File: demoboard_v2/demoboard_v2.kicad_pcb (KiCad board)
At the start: 2 copper layers, 95.9 x 90.2 mm, 44 parts, among them J1 PC104-8BIT, P1 3v3_IN_CONNECTOR, P2 CONN_01X03, P3 CONN_01X03, P4 CONN_01X02, P5 CONN_01X02, Q1 DMN2075U, U1 TMS570LS0714, U2 AP7331, U3 AP7361_3.3v, U4 INA301

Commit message: Beginning board layout.
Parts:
- added C24: 0.1µF, SFUSat:C_0402, F.Cu at (126.8, 28.0)
- added C25: 0.1µF, SFUSat:C_0402, F.Cu at (139.0, 43.0)
- added C26: 0.1µF, SFUSat:C_0402, F.Cu at (160.0, 43.0)
- added C27: 33pF, SFUSat:C_0402, F.Cu at (135.0, 88.0)
- added C28: 33pF, SFUSat:C_0402, F.Cu at (139.0, 87.0)
- added C29: 10nF, SFUSat:C_0402, F.Cu at (149.4, 96.1)
- added C30: 470µF, SFUSat:Supercap_v2, F.Cu at (164.1, 90.9)
- added C31: 0.1µF, SFUSat:C_0402, F.Cu at (307.4, 93.8)
- added C32: 0.1µF, SFUSat:C_0402, F.Cu at (293.9, 105.9)
- added D1: LED, SFUSat:LED_0603, F.Cu at (265.5, 113.6)
- added D2: PESD5Zx, SFUSat:PESD57zx, F.Cu at (317.2, 104.8)
- added D3: LED, SFUSat:L_0402, F.Cu at (330.9, 90.3)
- added FLASH0_RESET: TEST_1P, SFUSat:Test_Point, F.Cu at (119.0, 24.0)
- added FLASH0_WP: TEST_1P, SFUSat:Test_Point, F.Cu at (114.0, 24.0)
- added FLASH_CS: FLASH_CS, SFUSat:3x_01In_Header_v2, F.Cu at (140.0, 24.0)
- added FLASH_SPI: FLASH_SPI, SFUSat:3x_01In_Header_v2, F.Cu at (128.0, 24.0)
- added P6: UART, SFUSat:2x01In_Header_v2, F.Cu at (325.3, 61.4)
- added P7: OSC_FUALT_INJECT, SFUSat:2x01In_Header_v2, F.Cu at (136.0, 96.0)
- added Q2: DMN2075U, SFUSat:SOT23_DMN2075U, F.Cu at (246.3, 94.7)
- added Q3: 1v2_GOOD, SFUSat:SOT23_DMN2075U, F.Cu at (244.4, 102.6)
- added Q4: DMN2075U, SFUSat:SOT23_DMN2075U, F.Cu at (327.2, 105.6)
- added Q5: DMN2075U, SFUSat:SOT23_DMN2075U, F.Cu at (318.3, 91.3)
- added R10: 10k, SFUSat:R_0402, F.Cu at (129.2, 43.5)
- added R11: 10k, SFUSat:R_0402, F.Cu at (122.0, 38.0)
- added R12: 0, SFUSat:R_0402, F.Cu at (122.0, 34.8)
- added R13: 10k, SFUSat:R_0402, F.Cu at (121.6, 31.6)
- added R14: 10k, SFUSat:R_0402, F.Cu at (264.9, 66.0)
- added R15: 10k, SFUSat:R_0402, F.Cu at (255.8, 78.4)
- added R16: 0, SFUSat:R_0402, F.Cu at (259.1, 76.9)
- added R17: 10k, SFUSat:R_0402, F.Cu at (259.1, 81.8)
- added R18: 10k, SFUSat:R_0402, F.Cu at (253.9, 83.3)
- added R19: 10k, SFUSat:R_0402, F.Cu at (250.6, 85.3)
- added R20: 0, SFUSat:R_0402, F.Cu at (264.9, 70.9)
- added R21: 10k, SFUSat:R_0402, F.Cu at (268.2, 66.0)
- added R22: 200k, SFUSat:R_0402, F.Cu at (297.6, 110.5)
- added R23: 187k, SFUSat:R_0402, F.Cu at (304.3, 104.1)
- added R24: 100k, SFUSat:R_0402, F.Cu at (293.6, 110.5)
- added R25: 10k, SFUSat:R_0402, F.Cu at (112.0, 83.0)
- added R26: 10k, SFUSat:R_0402, F.Cu at (324.3, 95.9)
- added R27: 100k, SFUSat:R_0402, F.Cu at (304.3, 99.3)
- added R28: 100k, SFUSat:R_0402, F.Cu at (301.7, 109.0)
- added R29: 100k, SFUSat:R_0402, F.Cu at (308.4, 103.3)
- added R30: 100k, SFUSat:R_0402, F.Cu at (308.4, 98.4)
- added R5: 10K, SFUSat:R_0402, F.Cu at (262.3, 108.9)
- added R6: 100, SFUSat:R_0402, F.Cu at (258.1, 114.1)
- added R7: 10k, SFUSat:R_0402, F.Cu at (327.3, 117.5)
- added R8: 10k, SFUSat:R_0402, F.Cu at (330.9, 95.5)
- added R9: 100, SFUSat:R_0402, F.Cu at (327.5, 95.9)
- added RTC_SPI: RTC_SPI, SFUSat:4x01In_Header_v2, F.Cu at (143.0, 105.0)
- added SW1: SPST, SFUSat:Tact_SW_SMD_v2, F.Cu at (275.4, 107.7)
- added SW2: SPST, SFUSat:Tact_SW_SMD_v2, F.Cu at (291.0, 95.6)
- added U5: FLASH_IS25LP016D, SFUSat:SOT-8_208mil_medium, F.Cu at (128.0, 35.0)
- added U6: FLASH_IS25LP016D, SFUSat:SOT-8_208mil_medium, F.Cu at (138.0, 35.0)
- added U7: FLASH_IS25LP016D, SFUSat:SOT-8_208mil_medium, F.Cu at (148.0, 35.0)
- added U8: AB-RTCMC-EOA9-S3, SFUSat:RTC_AB-RTCMC_EA09_S3, F.Cu at (144.2, 95.2)
- added U9: TPS3110, SFUSat:SOT_23_6, F.Cu at (288.2, 105.5)
- added W10: RTC_OE, SFUSat:Test_Point, F.Cu at (133.0, 105.0)
- added W11: RTC_INT, SFUSat:Test_Point, F.Cu at (128.0, 105.0)
- added W12: nERROR, SFUSat:Test_Point, F.Cu at (299.1, 99.9)
- added W13: WD_TEST, SFUSat:Test_Point, F.Cu at (326.0, 90.5)
- added W14: RESET_TEST, SFUSat:Test_Point, F.Cu at (300.5, 93.9)
- added W3: TEST_1P, SFUSat:Test_Point, F.Cu at (259.1, 61.5)
- added W4: TEST_1P, SFUSat:Test_Point, F.Cu at (250.6, 69.0)
- added W5: TEST_1P, SFUSat:Test_Point, F.Cu at (244.4, 75.1)
- added W6: TEST_1P, SFUSat:Test_Point, F.Cu at (235.9, 82.7)
- added W7: AD1EVT1, SFUSat:Test_Point, F.Cu at (317.5, 118.1)
- added W8: GIOB2, SFUSat:Test_Point, F.Cu at (323.3, 118.1)
- added W9: CLKOUT, SFUSat:Test_Point, F.Cu at (313.1, 70.6)
- added Y1: XTAL, SFUSat:SMD_XTAL, F.Cu at (137.0, 80.0)
- P2: value CONN_01X03 -> INA_INPUT
- P3: value CONN_01X03 -> INA_GND
- P4: value CONN_01X02 -> INA_EN
- P5: value CONN_01X02 -> INA_OUTPUT
- moved C1 200.8 mm to (263.4, 104.2)
- moved C2 199.4 mm to (254.9, 114.6)
- moved 1uF1 191.9 mm to (258.7, 109.4)
- moved C4 190.5 mm to (253.0, 99.0)
- moved C9 190.1 mm to (255.5, 104.2)
- moved C8 188.4 mm to (262.3, 99.0)
- moved C10 184.4 mm to (250.8, 104.2)
- moved C7 183.7 mm to (262.3, 93.8)
- moved C3 181.9 mm to (257.6, 93.8)
- moved C5 179.6 mm to (236.9, 113.1)
- moved C13 178.6 mm to (241.6, 109.7)
- moved C11 178.5 mm to (257.6, 99.0)
- moved C6 178.3 mm to (241.6, 114.9)
- moved C12 176.9 mm to (246.3, 109.7)
- moved C16 176.9 mm to (251.0, 109.4)
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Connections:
- J1 pad 10A: Net-(J1-Pad10A) -> RF_PWM1
- J1 pad 11A: Net-(J1-Pad11A) -> RF_PWM2
- J1 pad 17B: Net-(J1-Pad17B) -> I2C_SDA
- J1 pad 18B: Net-(J1-Pad18B) -> I2C_SCL
- J1 pad 1B: 104_GND -> 104_In_GND
- J1 pad 22A: (no net) -> Net-(J1-Pad22A)
- J1 pad 23A: (no net) -> Net-(J1-Pad23A)
- J1 pad 24A: (no net) -> Net-(J1-Pad24A)
- J1 pad 25A: (no net) -> Net-(J1-Pad25A)
- J1 pad 26A: (no net) -> Net-(J1-Pad26A)
- J1 pad 27A: (no net) -> Net-(J1-Pad27A)
- J1 pad 28A: (no net) -> Net-(J1-Pad28A)
- J1 pad 29A: (no net) -> Net-(J1-Pad29A)
- J1 pad 30A: (no net) -> Net-(J1-Pad30A)
- J1 pad 31A: (no net) -> Net-(J1-Pad31A)
- J1 pad 31B: 104_GND -> 104_In_GND
- J1 pad 32A: (no net) -> 104_In_GND
- J1 pad 32B: 104_GND -> 104_In_GND
- J1 pad 5B: Net-(J1-Pad5B) -> UART_RX
- J1 pad 6B: Net-(J1-Pad6B) -> UART_TX
- J1 pad 8A: Net-(J1-Pad8A) -> RF_ADC1
- J1 pad 9A: Net-(J1-Pad9A) -> RF_ADC2
- P1 pad 2: GND -> Net-(P1-Pad2)
- U1 pad 1: (no net) -> Net-(U1-Pad1)
- U1 pad 105: Net-(U1-Pad105) -> FLASH0_CS
- U1 pad 107: (no net) -> Net-(U1-Pad107)
- U1 pad 118: (no net) -> Net-(U1-Pad118)
- U1 pad 124: (no net) -> Net-(U1-Pad124)
- U1 pad 125: (no net) -> Net-(U1-Pad125)
- U1 pad 126: (no net) -> WATCHDOG
- U1 pad 127: (no net) -> Net-(U1-Pad127)
- U1 pad 130: Net-(U1-Pad130) -> FLASH1_CS
- U1 pad 133: (no net) -> Net-(U1-Pad133)
- U1 pad 139: (no net) -> Net-(U1-Pad139)
- U1 pad 140: (no net) -> RF_PWM1
- U1 pad 141: (no net) -> RF_PWM2
- U1 pad 142: (no net) -> Net-(U1-Pad142)
- U1 pad 15: (no net) -> Net-(U1-Pad15)
- U1 pad 16: (no net) -> GIOA6
- U1 pad 2: (no net) -> Net-(U1-Pad2)
- U1 pad 22: (no net) -> Net-(U1-Pad22)
- U1 pad 24: Net-(U1-Pad24) -> RTC_CS
- U1 pad 25: Net-(U1-Pad25) -> RTC_CLK
- U1 pad 3: (no net) -> I2C_SCL
- U1 pad 30: Net-(U1-Pad30) -> RTC_MOSI
- U1 pad 31: Net-(U1-Pad31) -> RTC_MISO
- U1 pad 33: (no net) -> Net-(U1-Pad33)
- U1 pad 35: (no net) -> Net-(U1-Pad35)
- U1 pad 36: (no net) -> Net-(U1-Pad36)
- U1 pad 38: (no net) -> UART_RX
- U1 pad 39: (no net) -> UART_TX
- U1 pad 4: (no net) -> I2C_SDA
- U1 pad 40: Net-(U1-Pad40) -> FLASH2_CS
- U1 pad 46: Net-(U1-Pad46) -> MASTER_RESET
- U1 pad 5: (no net) -> Net-(U1-Pad5)
- U1 pad 55: (no net) -> Net-(U1-Pad55)
- U1 pad 58: (no net) -> Net-(U1-Pad58)
- U1 pad 59: (no net) -> Net-(U1-Pad59)
- U1 pad 60: (no net) -> RF_ADC1
- U1 pad 61: (no net) -> Net-(U1-Pad61)
- U1 pad 62: (no net) -> Net-(U1-Pad62)
- U1 pad 63: (no net) -> Net-(U1-Pad63)
- U1 pad 64: (no net) -> Net-(U1-Pad64)
- U1 pad 65: (no net) -> Net-(U1-Pad65)
- U1 pad 66: (no net) -> 3v3
- U1 pad 67: (no net) -> GND
- U1 pad 68: (no net) -> GND
- U1 pad 69: (no net) -> 3v3
- U1 pad 70: (no net) -> Net-(U1-Pad70)
- U1 pad 71: (no net) -> RF_ADC2
- U1 pad 72: (no net) -> Net-(U1-Pad72)
- U1 pad 73: (no net) -> INA_OUT
- U1 pad 74: (no net) -> Net-(U1-Pad74)
- U1 pad 75: (no net) -> Net-(U1-Pad75)
- U1 pad 76: (no net) -> Net-(U1-Pad76)
- U1 pad 77: (no net) -> Net-(U1-Pad77)
- U1 pad 78: (no net) -> Net-(U1-Pad78)
- U1 pad 79: (no net) -> Net-(U1-Pad79)
- U1 pad 80: (no net) -> Net-(U1-Pad80)
- U1 pad 81: (no net) -> Net-(U1-Pad81)
- U1 pad 82: (no net) -> Net-(U1-Pad82)
- U1 pad 83: (no net) -> Net-(U1-Pad83)
- U1 pad 84: (no net) -> Net-(U1-Pad84)
- U1 pad 85: (no net) -> Net-(U1-Pad85)
- U1 pad 86: (no net) -> Net-(U1-Pad86)
- U1 pad 9: (no net) -> Net-(U1-Pad9)
- U1 pad 92: (no net) -> Net-(U1-Pad92)
- U1 pad 93: Net-(U1-Pad93) -> FLASH_MOSI
- U1 pad 94: Net-(U1-Pad94) -> FLASH_MISO
- U1 pad 95: Net-(U1-Pad95) -> FLASH_CLK
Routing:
- net FLASH0_CS: track 0.00 -> 40.2 mm, vias 0 -> 1
- net FLASH_MISO: track 0.00 -> 28.3 mm, vias 0 -> 1
- net Net-(R12-Pad2): track 0.00 -> 15.8 mm
- net 3v3: track 9.03 -> 23.5 mm
- net FLASH_CLK: track 0.00 -> 8.78 mm
- net FLASH_MOSI: track 0.00 -> 7.72 mm
- net Net-(R10-Pad1): track 0.00 -> 5.03 mm
- net GND: track 4.42 -> 8.48 mm, vias 3 -> 6

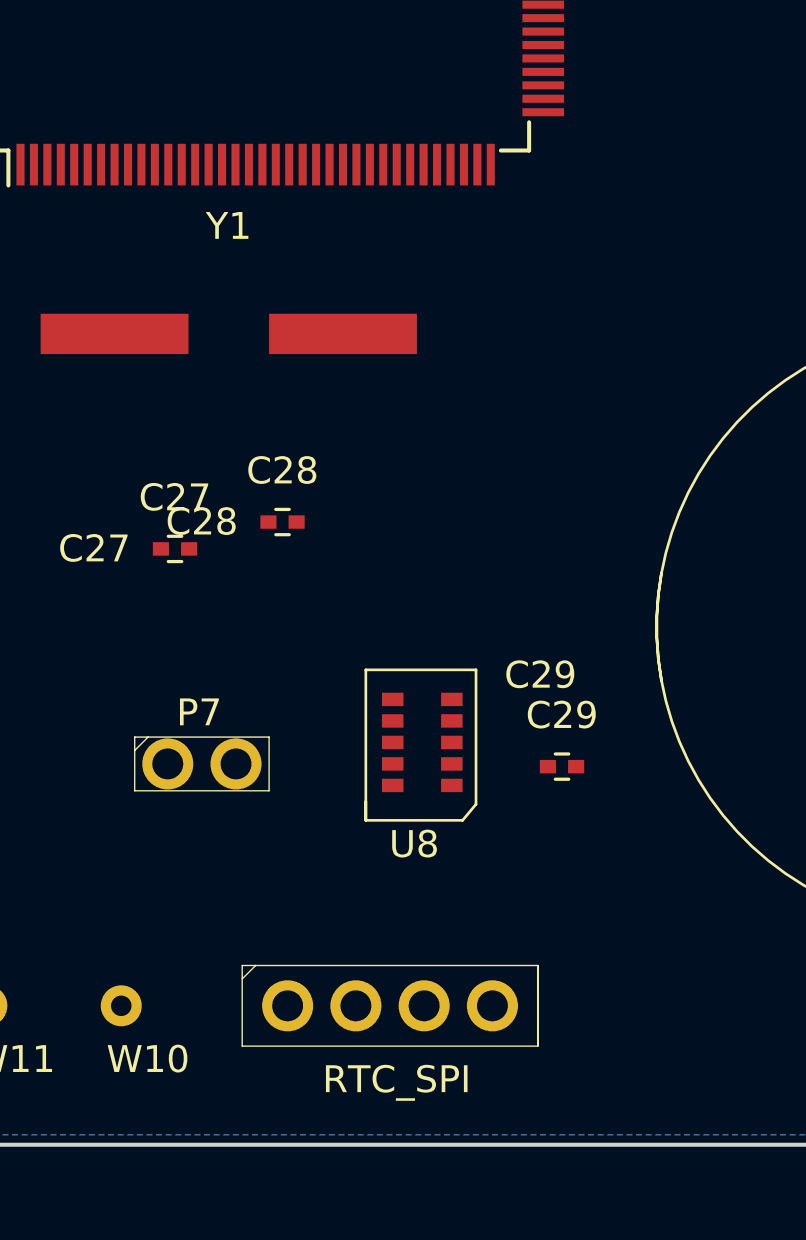
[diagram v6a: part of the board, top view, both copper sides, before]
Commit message: Connect RTC CS, CLK, MISO, MOSI
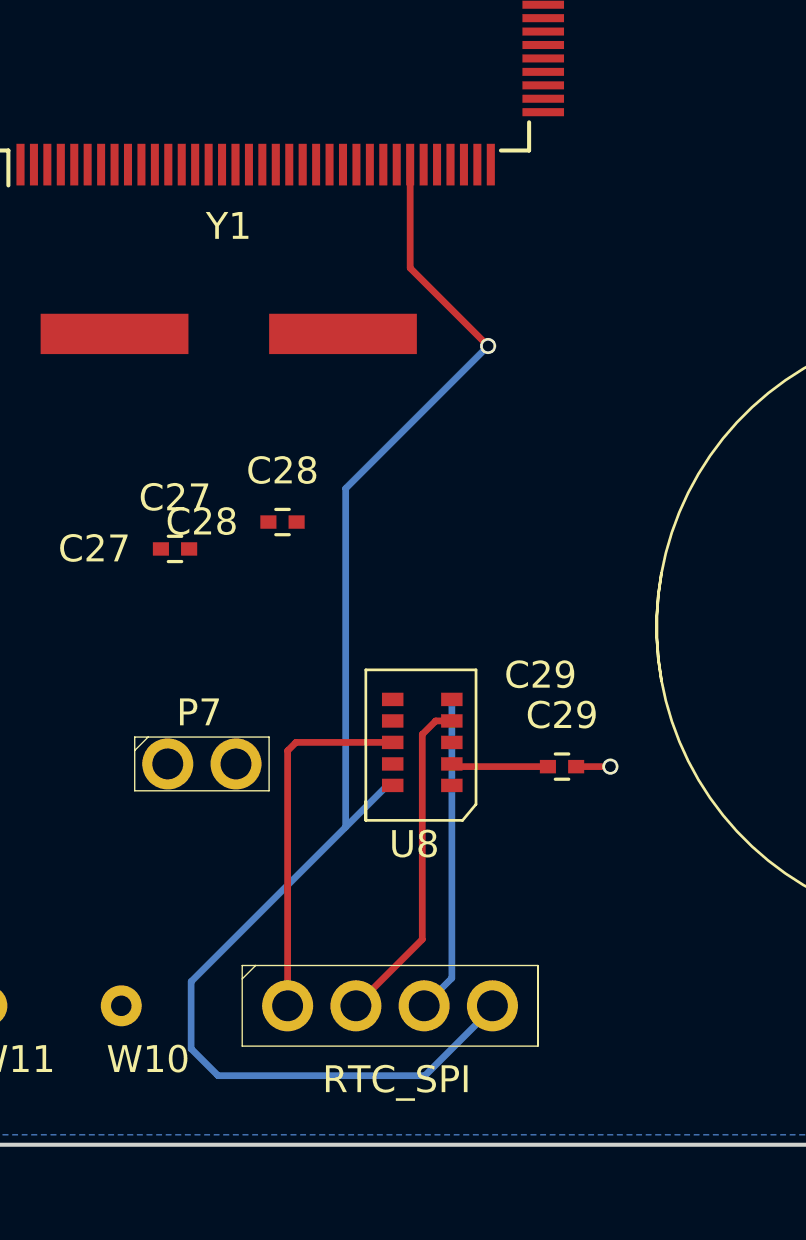
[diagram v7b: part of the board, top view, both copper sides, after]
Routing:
- net RTC_MOSI: track 0.00 -> 53.7 mm, vias 0 -> 1
- net RTC_CS: track 0.00 -> 13.5 mm
- net RTC_CLK: track 0.00 -> 12.4 mm
- net RTC_MISO: track 0.00 -> 11.8 mm, vias 0 -> 1
- net 3v3: track 23.5 -> 27.1 mm
- net GND: track 8.48 -> 9.76 mm, vias 6 -> 7
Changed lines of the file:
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@@
-(kicad_pcb (version 4) (host pcbnew 4.0.4-stable)
+(kicad_pcb (version 4) (host pcbnew 4.0.6)
   (general
     (links 278)
-    (no_connects 262)
+    (no_connects 258)
     (area 99.924999 19.924999 332.414286 121.19)
     (thickness 1.6)
     (drawings 4)
-    (tracks 63)
+    (tracks 90)
     (zones 0)
     (modules 113)
@@
   (gr_line (start 100 20) (end 100 110.17) (angle 90) (layer Edge.Cuts) (width 0.15))
   (gr_line (start 100 20) (end 195.89 20) (angle 90) (layer Edge.Cuts) (width 0.15))
+  (segment (start 148.875 96.1) (end 145.4 96.1) (width 0.25) (layer F.Cu) (net 1))
+  (segment (start 145.4 96.1) (end 145.3 96) (width 0.25) (layer F.Cu) (net 1))
   (segment (start 122.05 31.6) (end 122.05 32.45) (width 0.25) (layer F.Cu) (net 1))
   (segment (start 122.8 36.75) (end 122 37.55) (width 0.25) (layer F.Cu) (net 1))
@@
   (segment (start 124.275 66.75) (end 127.3 66.75) (width 0.25) (layer F.Cu) (net 1))
   (segment (start 131.25 52.3) (end 131.25 49.525) (width 0.25) (layer F.Cu) (net 1))
+  (segment (start 149.925 96.1) (end 151.2 96.1) (width 0.25) (layer F.Cu) (net 2))
+  (via (at 151.2 96.1) (size 0.6) (drill 0.4) (layers F.Cu B.Cu) (net 2))
   (segment (start 129.7 43.5) (end 130.9 43.5) (width 0.25) (layer F.Cu) (net 2))
   (via (at 130.9 43.5) (size 0.6) (drill 0.4) (layers F.Cu B.Cu) (net 2))
@@
   (segment (start 131.25 48.475) (end 131.25 47) (width 0.25) (layer F.Cu) (net 2))
   (via (at 131.25 47) (size 0.6) (drill 0.4) (layers F.Cu B.Cu) (net 2))
+  (via (at 144.27 105) (size 0.6) (drill 0.4) (layers F.Cu B.Cu) (net 99))
+  (segment (start 144.27 105) (end 145.3 103.97) (width 0.25) (layer B.Cu) (net 99))
+  (segment (start 145.3 103.97) (end 145.3 93.6) (width 0.25) (layer B.Cu) (net 99))
+  (segment (start 145.3 94.4) (end 144.7 94.4) (width 0.25) (layer F.Cu) (net 100))
+  (segment (start 144.2 102.53) (end 141.73 105) (width 0.25) (layer F.Cu) (net 100))
+  (segment (start 144.2 94.9) (end 144.2 102.53) (width 0.25) (layer F.Cu) (net 100))
+  (segment (start 144.7 94.4) (end 144.2 94.9) (width 0.25) (layer F.Cu) (net 100))
+  (segment (start 143.1 95.2) (end 139.5 95.2) (width 0.25) (layer F.Cu) (net 101))
+  (segment (start 139.19 95.51) (end 139.19 105) (width 0.25) (layer F.Cu) (net 101))
+  (segment (start 139.5 95.2) (end 139.19 95.51) (width 0.25) (layer F.Cu) (net 101))
+  (via (at 146.65 80.45) (size 0.6) (drill 0.4) (layers F.Cu B.Cu) (net 102))
+  (segment (start 143.75 73.7) (end 143.75 77.55) (width 0.25) (layer F.Cu) (net 102) (status 400000))
+  (segment (start 143.75 77.55) (end 146.65 80.45) (width 0.25) (layer F.Cu) (net 102))
+  (segment (start 141.35 98.35) (end 141.35 85.75) (width 0.25) (layer B.Cu) (net 102))
+  (segment (start 141.35 85.75) (end 146.65 80.45) (width 0.25) (layer B.Cu) (net 102))
+  (segment (start 146.65 80.45) (end 146.7 80.4) (width 0.25) (layer B.Cu) (net 102))
+  (segment (start 146.81 105) (end 146.81 105.09) (width 0.25) (layer B.Cu) (net 102) (status C00000))
+  (segment (start 146.81 105.09) (end 144.3 107.6) (width 0.25) (layer B.Cu) (net 102) (status 400000))
+  (segment (start 144.3 107.6) (end 136.6 107.6) (width 0.25) (layer B.Cu) (net 102))
+  (segment (start 136.6 107.6) (end 135.6 106.6) (width 0.25) (layer B.Cu) (net 102))
+  (segment (start 135.6 106.6) (end 135.6 104.1) (width 0.25) (layer B.Cu) (net 102))
+  (segment (start 135.6 104.1) (end 141.35 98.35) (width 0.25) (layer B.Cu) (net 102))
+  (segment (start 141.35 98.35) (end 142.9 96.8) (width 0.25) (layer B.Cu) (net 102))
   (segment (start 128.635 31.46) (end 128.635 27.175) (width 0.25) (layer F.Cu) (net 103))
   (segment (start 128.635 27.175) (end 125.46 24) (width 0.25) (layer F.Cu) (net 103))

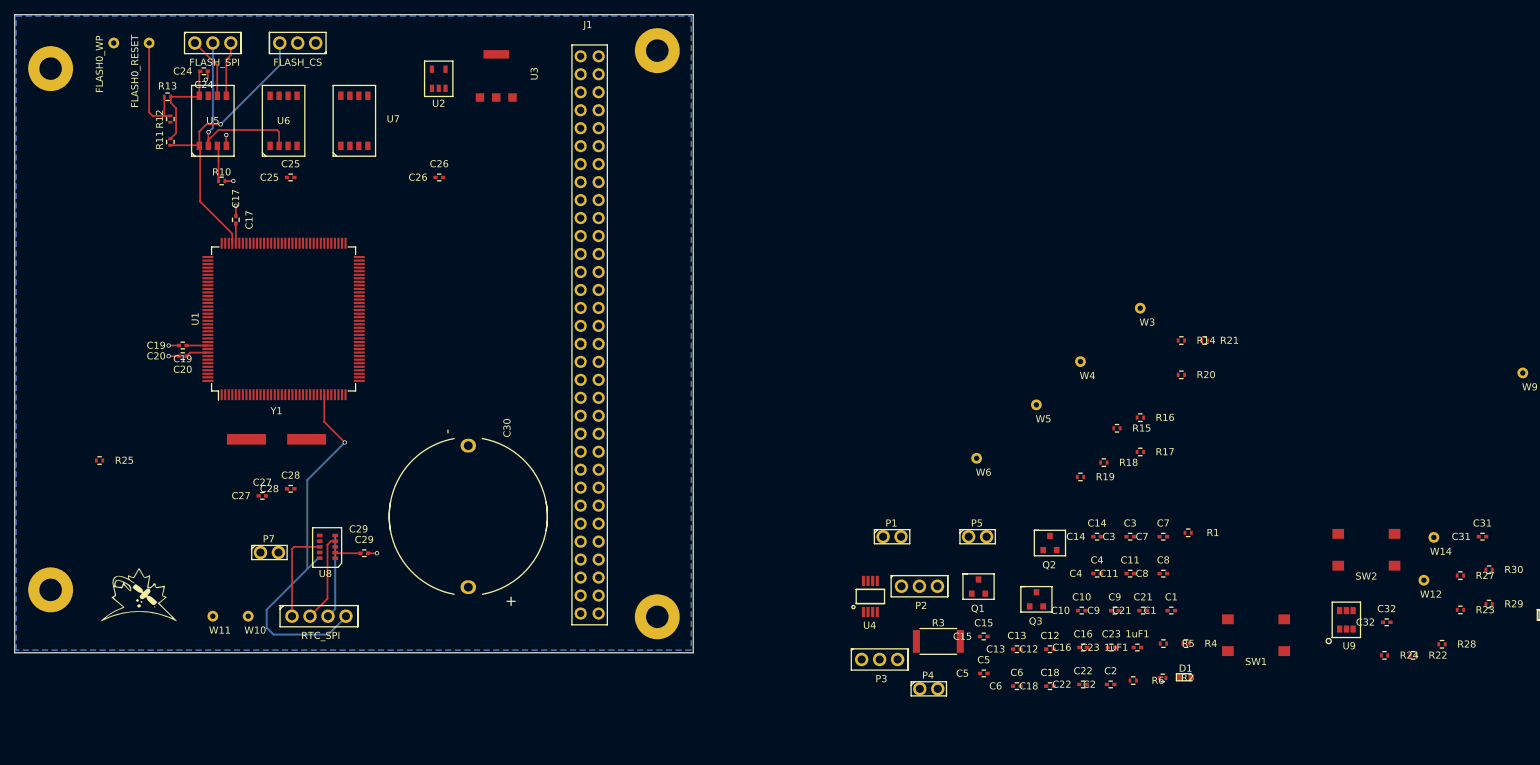
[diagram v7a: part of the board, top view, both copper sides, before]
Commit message: Checked design rules, placed decoupling for MCU. Beginning placement
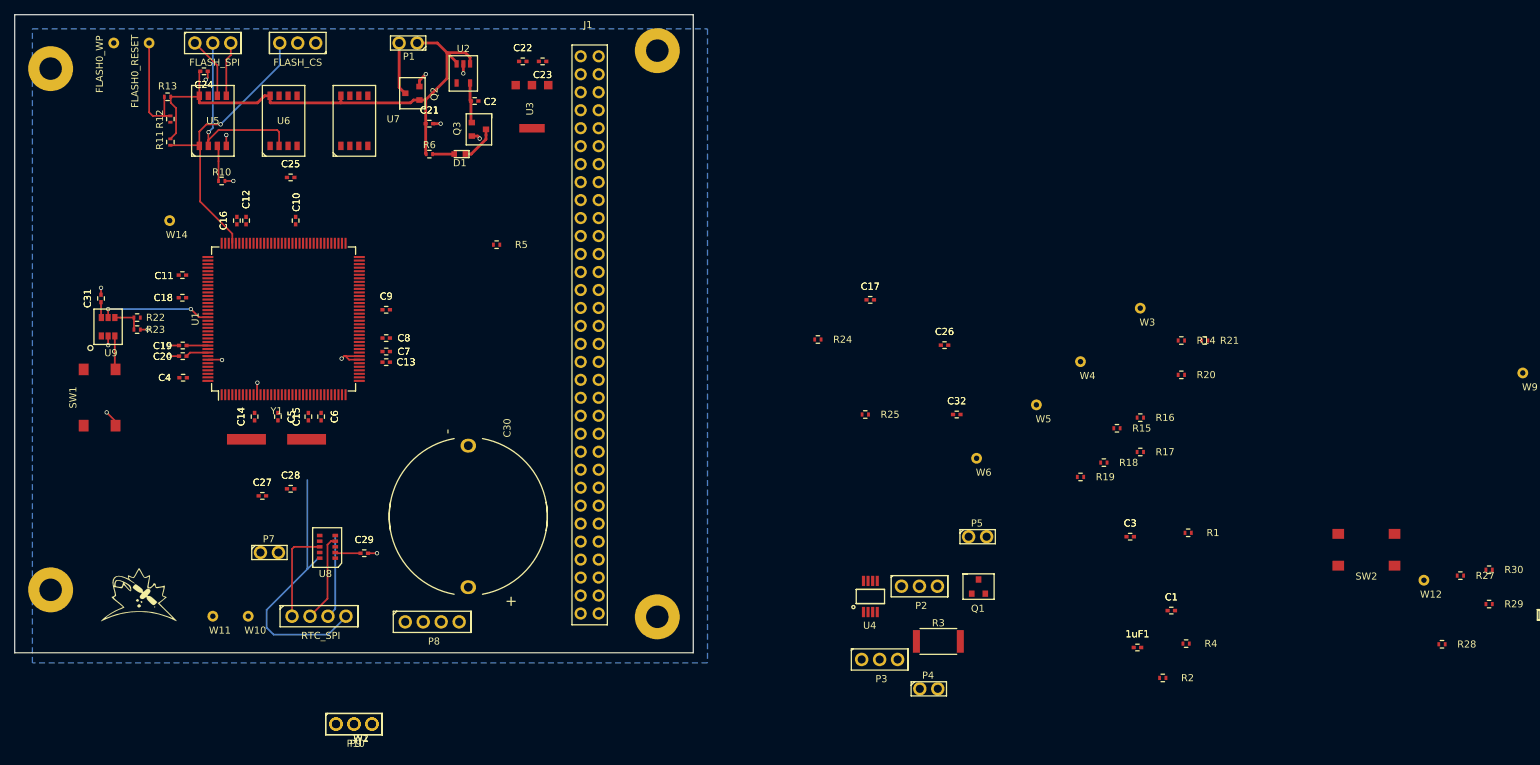
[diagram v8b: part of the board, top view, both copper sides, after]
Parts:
- added P10: FLASH_CS, SFUSat:3x_01In_Header_v2, F.Cu at (147.9, 120.2)
- added P8: RTC_SPI, SFUSat:4x01In_Header_v2, F.Cu at (159.0, 105.8)
- added P9: FLASH_SPI, SFUSat:3x_01In_Header_v2, F.Cu at (147.9, 120.2)
- added W1, W2: TEST_1P, SFUSat:Test_Point, F.Cu at (147.9, 120.2)
- moved C31 198.1 mm to (112.2, 60.1), turned to 90 degrees
- moved R23 191.1 mm to (117.3, 64.5)
- moved R22 186.5 mm to (117.3, 62.8), turned to 180 degrees
- moved W14 184.2 mm to (121.9, 49.1)
- moved U9 179.8 mm to (113.2, 64.1)
- moved SW1 166.8 mm to (112.0, 74.1), turned to 270 degrees
- moved C11 140.4 mm to (123.7, 56.8), turned to 180 degrees
- moved C18 134.3 mm to (123.7, 60.0), turned to 180 degrees
- moved C16 133.9 mm to (131.4, 49.1), turned to 90 degrees
- moved C4 132.1 mm to (123.8, 71.3), turned to 180 degrees
- moved C12 128.7 mm to (132.7, 49.1), turned to 90 degrees
- moved D1 126.4 mm to (162.9, 39.7), turned to 180 degrees
- moved R6 124.2 mm to (158.6, 39.7)
- moved C10 124.0 mm to (139.7, 49.1), turned to 90 degrees
- moved C21 122.1 mm to (158.6, 35.4)
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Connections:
- C1 pad 2: 3v3 -> 1v2
- C10 pad 1: 3v3 -> 1v2
- C11 pad 1: 3v3 -> 1v2
- C12 pad 1: 3v3 -> 1v2
- C13 pad 1: 3v3 -> 1v2
- C3 pad 1: 3v3 -> 1v2
- C4 pad 1: 3v3 -> 1v2
- C5 pad 1: 3v3 -> 1v2
- C6 pad 1: 3v3 -> 1v2
- C7 pad 1: 3v3 -> 1v2
- C8 pad 1: 3v3 -> 1v2
- C9 pad 1: 3v3 -> 1v2
- R6 pad 1: Net-(R6-Pad1) -> 3v3
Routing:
- net 3v3: track 27.1 -> 89.0 mm
- net GND: track 9.76 -> 28.4 mm, vias 7 -> 17
- net WATCHDOG: track 0.00 -> 15.8 mm, vias 0 -> 2
- net RTC_MOSI: track 53.7 -> 38.2 mm, vias 1 -> 0
- net Net-(P1-Pad2): track 0.00 -> 7.49 mm
- net 1v2: track 0.00 -> 5.69 mm
- net Net-(D1-Pad1): track 0.00 -> 5.17 mm
- net Net-(SW1-Pad1): track 0.00 -> 4.77 mm
- net Net-(R22-Pad2): track 0.00 -> 4.40 mm
- net Net-(D1-Pad2): track 0.00 -> 3.05 mm
